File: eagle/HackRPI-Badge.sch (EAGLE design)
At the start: 42 parts, among them J1 FTDI_BASICPTH, J2 SOLDERJUMPERTRACE-PTH, U2 3.3V, U4 74595, U5 74595, U6 74595, U7 74165DT, U8 AT25SF041

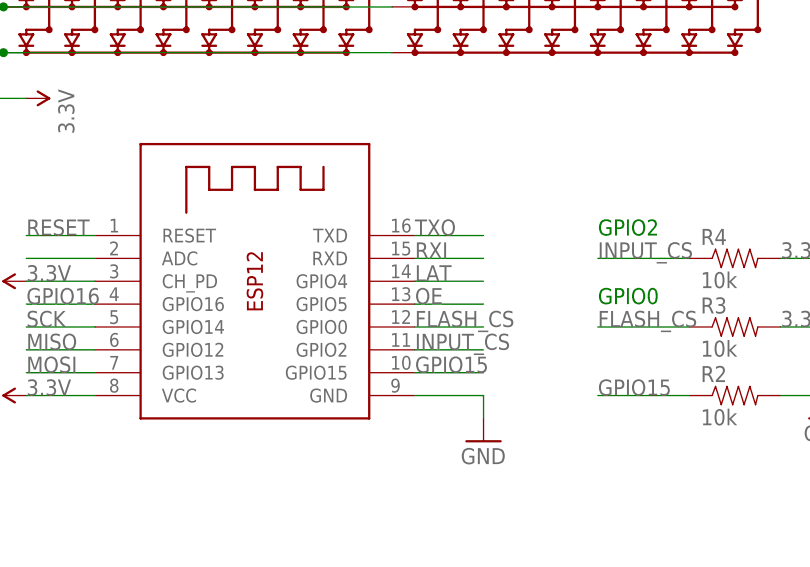
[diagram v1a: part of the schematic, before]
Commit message: Fixed ESP12 pinout
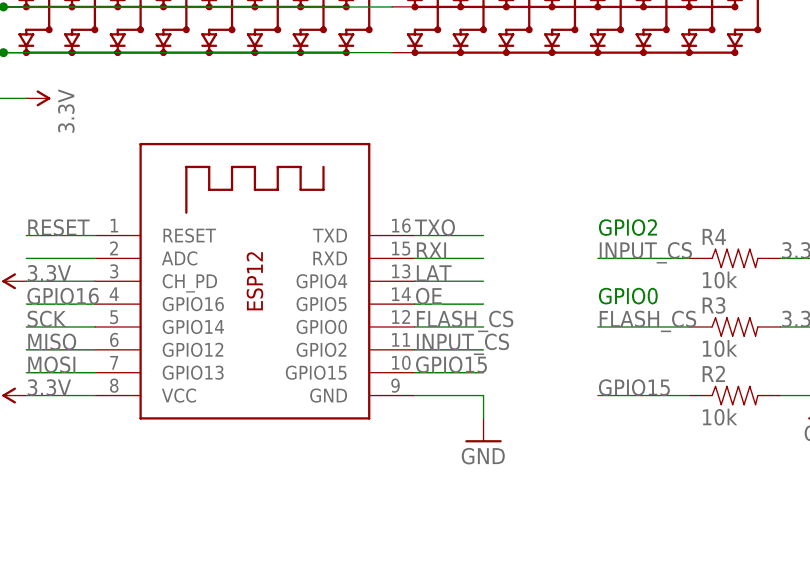
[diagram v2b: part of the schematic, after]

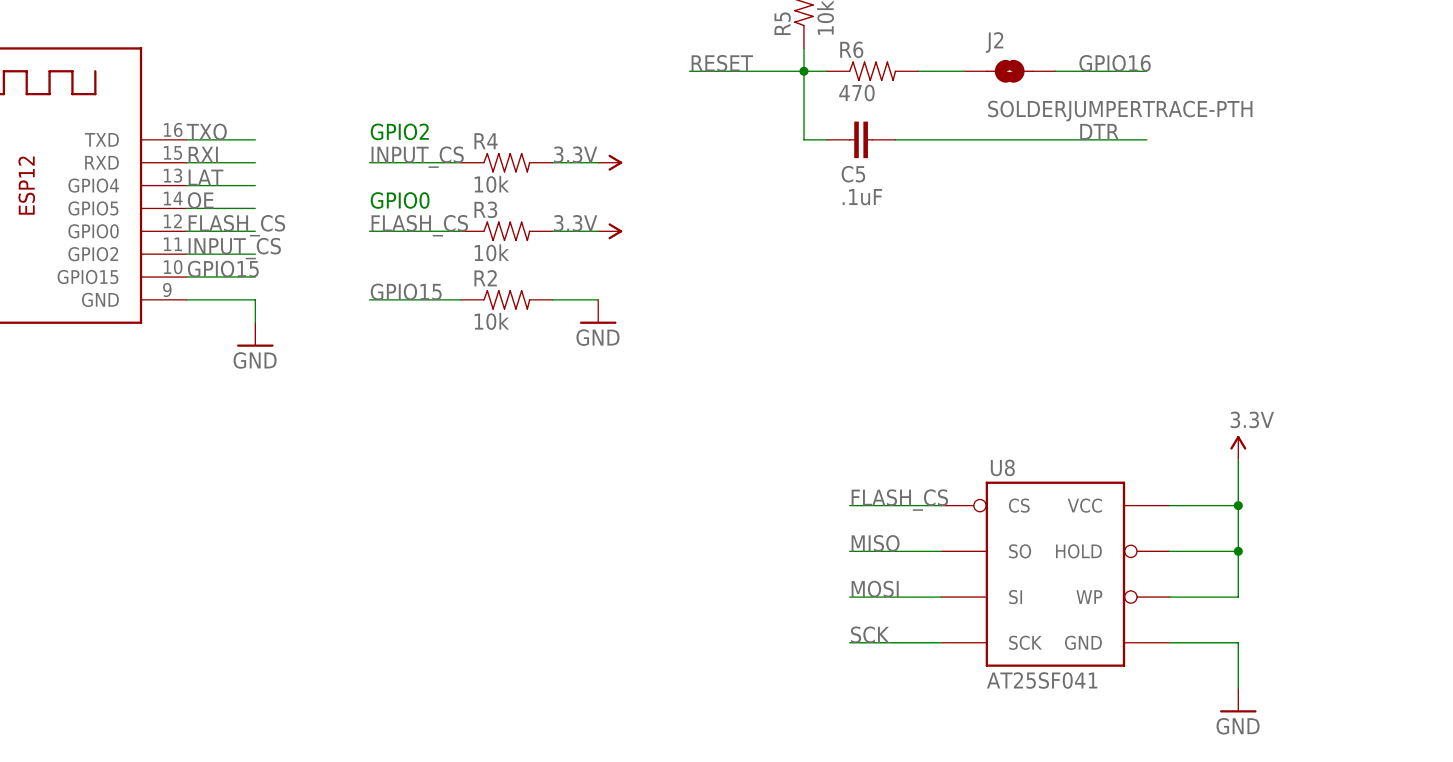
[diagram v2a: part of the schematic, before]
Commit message: Removed external flash memory from badge (ESP-12 module has plenty of flash onboard)
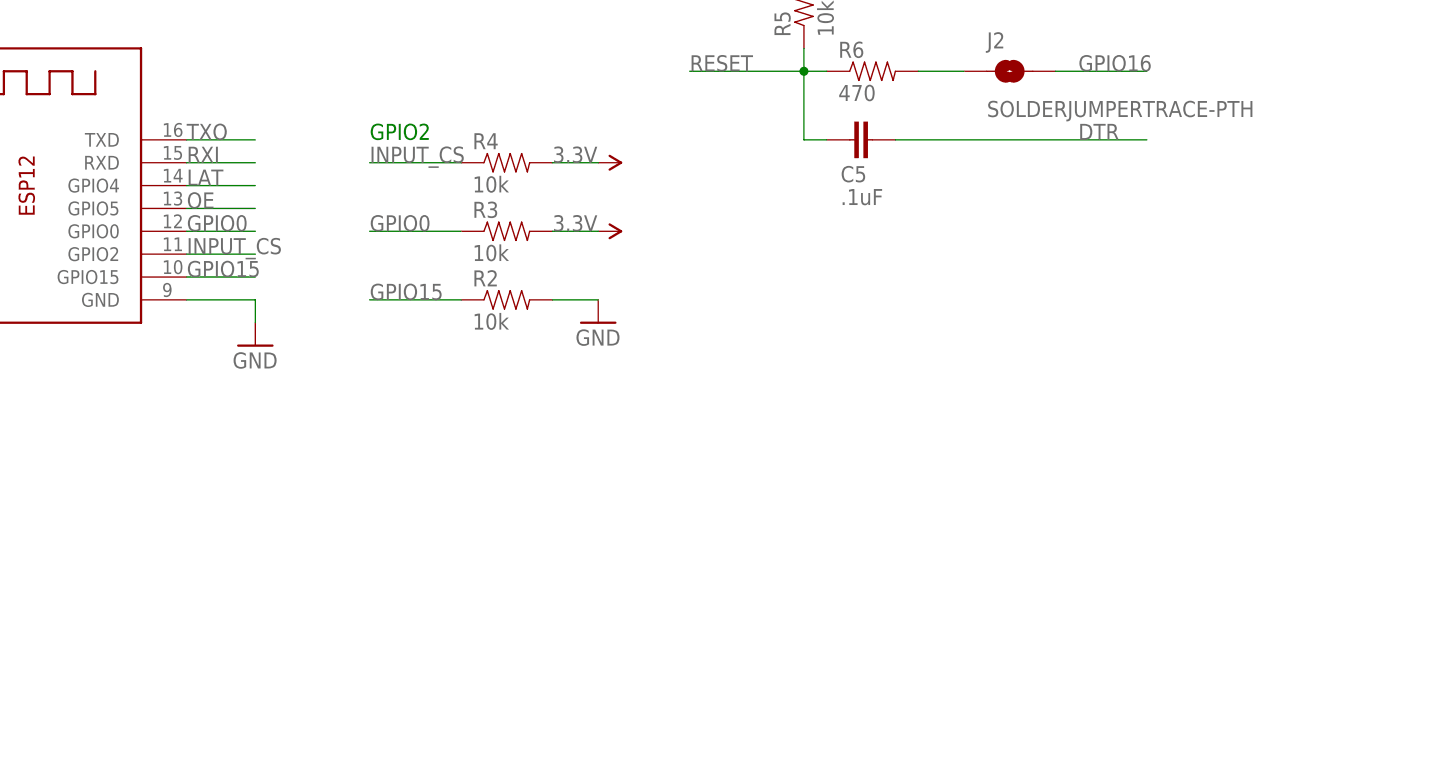
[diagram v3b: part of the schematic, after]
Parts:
- removed U8: AT25SF041, SparkFun-DigitalIC:AT25FS010
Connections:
- removed net FLASH_CS: R3.1, U1.GPIO0, U8.CS
- new net GPIO0: R3.1, U1.GPIO0
- net 3.3V: no longer U8.HOLD, U8.VCC, U8.WP
- net GND: no longer U8.GND
- net MISO: no longer U8.SO
- net MOSI: no longer U8.SI
- net SCK: no longer U8.SCK
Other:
- note removed: "GPIO0"
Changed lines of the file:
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@@
 <part name="GND17" library="SparkFun-Aesthetics" deviceset="GND" device=""/>
 <part name="SUPPLY23" library="SparkFun-Aesthetics" deviceset="V_BATT" device=""/>
-<part name="SUPPLY24" library="SparkFun-Aesthetics" deviceset="3.3V" device=""/>
-<part name="GND18" library="SparkFun-Aesthetics" deviceset="GND" device=""/>
-<part name="U8" library="SparkFun-DigitalIC" deviceset="AT25FS010" device="" value="AT25SF041">
-<attribute name="PARTNO" value="AT25SF041-SSHD-T"/>
-</part>
 </parts>
 <sheets>
 <sheet>
 <plain>
-<text x="38.1" y="-2.54" size="1.778" layer="91">GPIO0</text>
 <text x="38.1" y="5.08" size="1.778" layer="91">GPIO2</text>
 </plain>
@@
 <instance part="GND17" gate="1" x="-190.5" y="12.7"/>
 <instance part="SUPPLY23" gate="G$1" x="-190.5" y="45.72"/>
-<instance part="SUPPLY24" gate="G$1" x="134.62" y="-30.48"/>
-<instance part="GND18" gate="1" x="134.62" y="-58.42"/>
-<instance part="U8" gate="G$1" x="114.3" y="-40.64">
-<attribute name="PARTNO" x="114.3" y="-40.64" size="1.778" layer="96" display="off"/>
-</instance>
 </instances>
 <busses>
@@
 </segment>
 <segment>
-<wire x1="101.6" y1="-50.8" x2="91.44" y2="-50.8" width="0.1524" layer="91"/>
-<label x="91.44" y="-50.8" size="1.778" layer="95"/>
-<pinref part="U8" gate="G$1" pin="SCK"/>
-</segment>
-<segment>
 <pinref part="U7" gate="A" pin="CLK"/>
 <wire x1="104.14" y1="88.9" x2="91.44" y2="88.9" width="0.1524" layer="91"/>
@@
 <label x="91.44" y="81.28" size="1.778" layer="95"/>
 </segment>
-<segment>
-<wire x1="91.44" y1="-40.64" x2="101.6" y2="-40.64" width="0.1524" layer="91"/>
-<label x="91.44" y="-40.64" size="1.778" layer="95"/>
-<pinref part="U8" gate="G$1" pin="SO"/>
-</segment>
 </net>
 <net name="MOSI" class="0">
@@
 <wire x1="-111.76" y1="172.72" x2="-119.38" y2="172.72" width="0.1524" layer="91"/>
 <label x="-119.38" y="172.72" size="1.778" layer="95"/>
-</segment>
-<segment>
-<wire x1="101.6" y1="-45.72" x2="91.44" y2="-45.72" width="0.1524" layer="91"/>
-<label x="91.44" y="-45.72" size="1.778" layer="95"/>
-<pinref part="U8" gate="G$1" pin="SI"/>
 </segment>
 </net>
@@
 <wire x1="-88.9" y1="53.34" x2="-88.9" y2="50.8" width="0.1524" layer="91"/>
 </segment>
-<segment>
-<wire x1="127" y1="-35.56" x2="134.62" y2="-35.56" width="0.1524" layer="91"/>
-<wire x1="134.62" y1="-35.56" x2="134.62" y2="-30.48" width="0.1524" layer="91"/>
-<pinref part="SUPPLY24" gate="G$1" pin="3.3V"/>
-<wire x1="127" y1="-45.72" x2="134.62" y2="-45.72" width="0.1524" layer="91"/>
-<wire x1="134.62" y1="-45.72" x2="134.62" y2="-40.64" width="0.1524" layer="91"/>
-<junction x="134.62" y="-35.56"/>
-<pinref part="U8" gate="G$1" pin="WP"/>
-<pinref part="U8" gate="G$1" pin="VCC"/>
-<pinref part="U8" gate="G$1" pin="HOLD"/>
-<wire x1="134.62" y1="-40.64" x2="134.62" y2="-35.56" width="0.1524" layer="91"/>
-<wire x1="127" y1="-40.64" x2="134.62" y2="-40.64" width="0.1524" layer="91"/>
-<junction x="134.62" y="-40.64"/>
-</segment>
 </net>
 <net name="GND" class="1">
@@
 <pinref part="GND17" gate="1" pin="GND"/>
 </segment>
-<segment>
-<wire x1="127" y1="-50.8" x2="134.62" y2="-50.8" width="0.1524" layer="91"/>
-<wire x1="134.62" y1="-50.8" x2="134.62" y2="-55.88" width="0.1524" layer="91"/>
-<pinref part="GND18" gate="1" pin="GND"/>
-<pinref part="U8" gate="G$1" pin="GND"/>
-</segment>
 </net>
 <net name="INPUT_CS" class="0">
@@
 </segment>
 </net>
-<net name="FLASH_CS" class="0">
+<net name="GPIO0" class="0">
 <segment>
 <pinref part="U1" gate="G$1" pin="GPIO0"/>
@@
 <label x="38.1" y="-5.08" size="1.778" layer="95"/>
 </segment>
-<segment>
-<wire x1="101.6" y1="-35.56" x2="91.44" y2="-35.56" width="0.1524" layer="91"/>
-<label x="91.44" y="-35.56" size="1.778" layer="95"/>
-<pinref part="U8" gate="G$1" pin="CS"/>
-</segment>
-</net>
+</net>

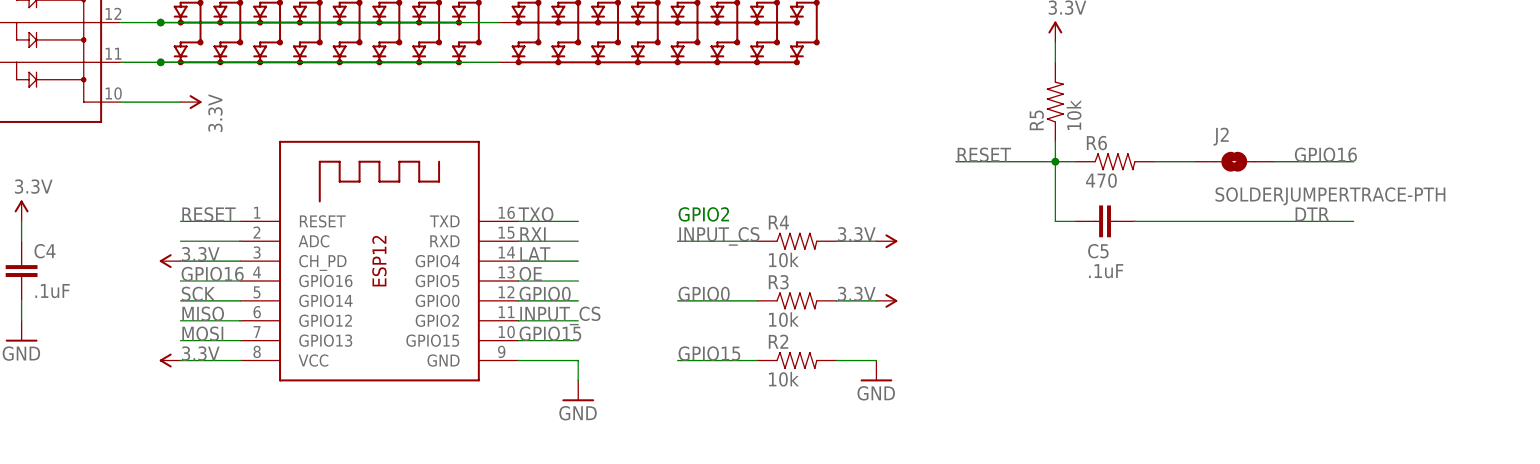
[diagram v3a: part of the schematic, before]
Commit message: Moved buttons, changed some pin assignments, added input shift register source
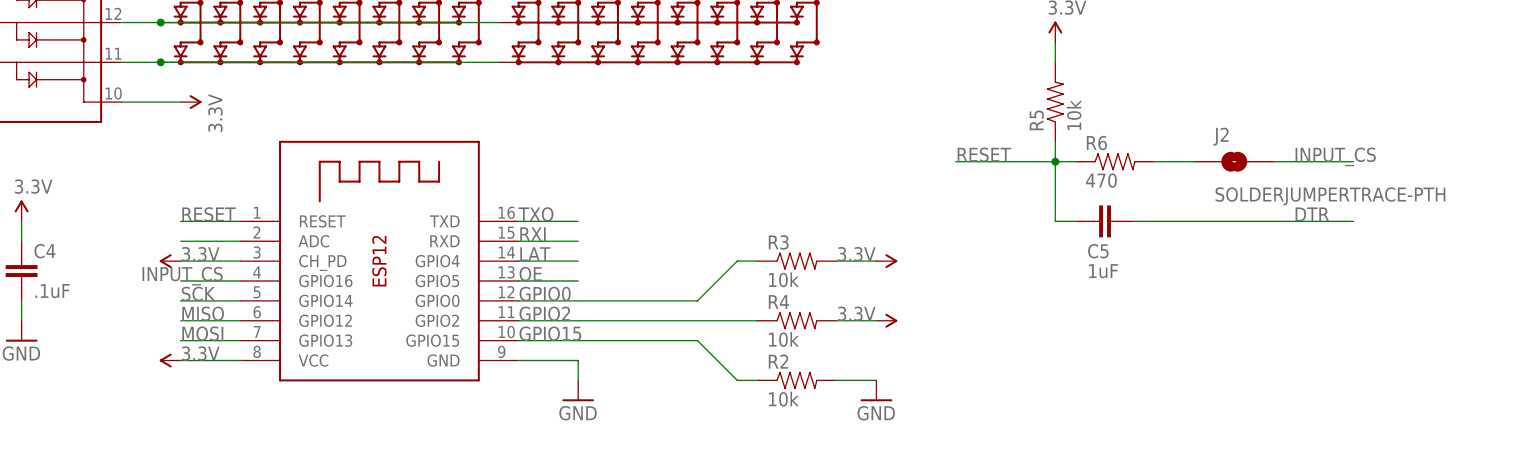
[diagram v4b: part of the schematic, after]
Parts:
- C5: value .1uF -> 1uF; PARTNO CC0603ZRY5V9BB104 -> (none)
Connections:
- removed net GPIO16: J2.2, U1.GPIO16
- new net GPIO2: R4.1, U1.GPIO2
- net INPUT_CS: now also J2.2, U1.GPIO16; no longer R4.1, U1.GPIO2
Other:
- note removed: "GPIO2"
- moved on the sheet: R2, R3, R4
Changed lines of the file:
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@@
 </part>
 <part name="J1" library="SparkFun-Connectors" deviceset="FTDI_BASIC" device="PTH"/>
-<part name="C5" library="SparkFun-Capacitors" deviceset="CAP" device="0603-CAP" value=".1uF">
-<attribute name="PARTNO" value="CC0603ZRY5V9BB104"/>
-</part>
+<part name="C5" library="SparkFun-Capacitors" deviceset="CAP" device="0603-CAP" value="1uF"/>
 <part name="J2" library="SparkFun-Retired" deviceset="SOLDERJUMPER" device="TRACE-PTH"/>
 <part name="U7" library="mylib" deviceset="74*165" device="DT">
@@
 <sheet>
 <plain>
-<text x="38.1" y="5.08" size="1.778" layer="91">GPIO2</text>
 </plain>
 <instances>
@@
 <attribute name="VALUE" x="-119.38" y="132.08" size="1.778" layer="96"/>
 </instance>
-<instance part="R2" gate="G$1" x="53.34" y="-12.7">
-<attribute name="PARTNO" x="53.34" y="-12.7" size="1.778" layer="96" display="off"/>
-</instance>
-<instance part="GND11" gate="1" x="63.5" y="-15.24"/>
+<instance part="R2" gate="G$1" x="53.34" y="-15.24">
+<attribute name="PARTNO" x="53.34" y="-15.24" size="1.778" layer="96" display="off"/>
+</instance>
+<instance part="GND11" gate="1" x="63.5" y="-17.78"/>
 <instance part="SUPPLY1" gate="G$1" x="-25.4" y="0" smashed="yes" rot="R90">
 <attribute name="VALUE" x="-25.4" y="0" size="1.778" layer="96"/>
 </instance>
-<instance part="SUPPLY16" gate="G$1" x="63.5" y="-5.08" smashed="yes" rot="R270">
-<attribute name="VALUE" x="58.42" y="-5.08" size="1.778" layer="96"/>
-</instance>
-<instance part="R3" gate="G$1" x="53.34" y="-5.08">
-<attribute name="PARTNO" x="53.34" y="-5.08" size="1.778" layer="96" display="off"/>
-</instance>
-<instance part="R4" gate="G$1" x="53.34" y="2.54">
-<attribute name="PARTNO" x="53.34" y="2.54" size="1.778" layer="96" display="off"/>
-</instance>
-<instance part="SUPPLY17" gate="G$1" x="63.5" y="2.54" smashed="yes" rot="R270">
-<attribute name="VALUE" x="58.42" y="2.54" size="1.778" layer="96"/>
+<instance part="SUPPLY16" gate="G$1" x="63.5" y="0" smashed="yes" rot="R270">
+<attribute name="VALUE" x="58.42" y="0" size="1.778" layer="96"/>
+</instance>
+<instance part="R3" gate="G$1" x="53.34" y="0">
+<attribute name="PARTNO" x="53.34" y="0" size="1.778" layer="96" display="off"/>
+</instance>
+<instance part="R4" gate="G$1" x="53.34" y="-7.62">
+<attribute name="PARTNO" x="53.34" y="-7.62" size="1.778" layer="96" display="off"/>
+</instance>
+<instance part="SUPPLY17" gate="G$1" x="63.5" y="-7.62" smashed="yes" rot="R270">
+<attribute name="VALUE" x="58.42" y="-7.62" size="1.778" layer="96"/>
 </instance>
 <instance part="R5" gate="G$1" x="86.36" y="20.32" rot="R90">
@@
 <attribute name="NAME" x="90.424" y="0.381" size="1.778" layer="95"/>
 <attribute name="VALUE" x="90.424" y="-2.159" size="1.778" layer="96"/>
-<attribute name="PARTNO" x="93.98" y="5.08" size="1.778" layer="96" display="off"/>
 </instance>
 <instance part="J2" gate="1" x="109.22" y="12.7"/>
@@
 </segment>
 <segment>
-<wire x1="58.42" y1="-5.08" x2="63.5" y2="-5.08" width="0.1524" layer="91"/>
+<wire x1="58.42" y1="0" x2="63.5" y2="0" width="0.1524" layer="91"/>
 <pinref part="SUPPLY16" gate="G$1" pin="3.3V"/>
 <pinref part="R3" gate="G$1" pin="2"/>
 </segment>
 <segment>
-<wire x1="58.42" y1="2.54" x2="63.5" y2="2.54" width="0.1524" layer="91"/>
+<wire x1="58.42" y1="-7.62" x2="63.5" y2="-7.62" width="0.1524" layer="91"/>
 <pinref part="SUPPLY17" gate="G$1" pin="3.3V"/>
 <pinref part="R4" gate="G$1" pin="2"/>
@@
 <pinref part="R2" gate="G$1" pin="2"/>
 <pinref part="GND11" gate="1" pin="GND"/>
-<wire x1="63.5" y1="-12.7" x2="58.42" y2="-12.7" width="0.1524" layer="91"/>
+<wire x1="63.5" y1="-15.24" x2="58.42" y2="-15.24" width="0.1524" layer="91"/>
 </segment>
 <segment>
@@
 <net name="INPUT_CS" class="0">
 <segment>
-<pinref part="U1" gate="G$1" pin="GPIO2"/>
-<wire x1="17.78" y1="-7.62" x2="25.4" y2="-7.62" width="0.1524" layer="91"/>
-<label x="17.78" y="-7.62" size="1.778" layer="95"/>
-</segment>
-<segment>
-<wire x1="38.1" y1="2.54" x2="48.26" y2="2.54" width="0.1524" layer="91"/>
-<pinref part="R4" gate="G$1" pin="1"/>
-<label x="38.1" y="2.54" size="1.778" layer="95"/>
-</segment>
-<segment>
 <pinref part="U7" gate="A" pin="CLK_INH"/>
 <wire x1="104.14" y1="86.36" x2="91.44" y2="86.36" width="0.1524" layer="91"/>
 <label x="91.44" y="86.36" size="1.778" layer="95"/>
 </segment>
+<segment>
+<pinref part="U1" gate="G$1" pin="GPIO16"/>
+<wire x1="-17.78" y1="-2.54" x2="-25.4" y2="-2.54" width="0.1524" layer="91"/>
+<label x="-30.48" y="-2.54" size="1.778" layer="95"/>
+</segment>
+<segment>
+<wire x1="124.46" y1="12.7" x2="114.3" y2="12.7" width="0.1524" layer="91"/>
+<label x="116.84" y="12.7" size="1.778" layer="95"/>
+<pinref part="J2" gate="1" pin="2"/>
+</segment>
 </net>
 <net name="GPIO0" class="0">
 <segment>
 <pinref part="U1" gate="G$1" pin="GPIO0"/>
-<wire x1="17.78" y1="-5.08" x2="25.4" y2="-5.08" width="0.1524" layer="91"/>
 <label x="17.78" y="-5.08" size="1.778" layer="95"/>
-</segment>
-<segment>
-<wire x1="38.1" y1="-5.08" x2="48.26" y2="-5.08" width="0.1524" layer="91"/>
+<wire x1="17.78" y1="-5.08" x2="40.64" y2="-5.08" width="0.1524" layer="91"/>
+<wire x1="40.64" y1="-5.08" x2="45.72" y2="0" width="0.1524" layer="91"/>
+<wire x1="45.72" y1="0" x2="48.26" y2="0" width="0.1524" layer="91"/>
 <pinref part="R3" gate="G$1" pin="1"/>
-<label x="38.1" y="-5.08" size="1.778" layer="95"/>
 </segment>
 </net>
@@
 <segment>
 <pinref part="U1" gate="G$1" pin="GPIO15"/>
-<wire x1="17.78" y1="-10.16" x2="25.4" y2="-10.16" width="0.1524" layer="91"/>
 <label x="17.78" y="-10.16" size="1.778" layer="95"/>
-</segment>
-<segment>
+<wire x1="17.78" y1="-10.16" x2="40.64" y2="-10.16" width="0.1524" layer="91"/>
+<wire x1="40.64" y1="-10.16" x2="45.72" y2="-15.24" width="0.1524" layer="91"/>
 <pinref part="R2" gate="G$1" pin="1"/>
-<wire x1="48.26" y1="-12.7" x2="38.1" y2="-12.7" width="0.1524" layer="91"/>
-<label x="38.1" y="-12.7" size="1.778" layer="95"/>
-</segment>
-</net>
-<net name="GPIO16" class="0">
-<segment>
-<pinref part="U1" gate="G$1" pin="GPIO16"/>
-<wire x1="-17.78" y1="-2.54" x2="-25.4" y2="-2.54" width="0.1524" layer="91"/>
-<label x="-25.4" y="-2.54" size="1.778" layer="95"/>
-</segment>
-<segment>
-<wire x1="124.46" y1="12.7" x2="114.3" y2="12.7" width="0.1524" layer="91"/>
-<label x="116.84" y="12.7" size="1.778" layer="95"/>
-<pinref part="J2" gate="1" pin="2"/>
+<wire x1="48.26" y1="-15.24" x2="45.72" y2="-15.24" width="0.1524" layer="91"/>
 </segment>
 </net>
@@
 </segment>
 </net>
+<net name="GPIO2" class="0">
+<segment>
+<pinref part="U1" gate="G$1" pin="GPIO2"/>
+<label x="17.78" y="-7.62" size="1.778" layer="95"/>
+<pinref part="R4" gate="G$1" pin="1"/>
+<wire x1="17.78" y1="-7.62" x2="48.26" y2="-7.62" width="0.1524" layer="91"/>
+</segment>
+</net>

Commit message: Tied GPIO0 to DTR, changed deep sleep jumper to normally open (necessary for programming)
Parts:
- J2: value SOLDERJUMPERTRACE-PTH -> SOLDERJUMPERPTH; device SparkFun-Retired:SOLDERJUMPERTRACE-PTH -> SparkFun-Retired:SOLDERJUMPERPTH
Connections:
- removed net GPIO0: R3.1, U1.GPIO0
- net DTR: now also R3.1, U1.GPIO0
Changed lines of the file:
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@@
 <part name="J1" library="SparkFun-Connectors" deviceset="FTDI_BASIC" device="PTH"/>
 <part name="C5" library="SparkFun-Capacitors" deviceset="CAP" device="0603-CAP" value="1uF"/>
-<part name="J2" library="SparkFun-Retired" deviceset="SOLDERJUMPER" device="TRACE-PTH"/>
+<part name="J2" library="SparkFun-Retired" deviceset="SOLDERJUMPER" device="PTH" value="SOLDERJUMPERPTH"/>
 <part name="U7" library="mylib" deviceset="74*165" device="DT">
 <attribute name="PARTNO" value="MC74HC165ADTR2G"/>
@@
 </segment>
 </net>
-<net name="GPIO0" class="0">
-<segment>
-<pinref part="U1" gate="G$1" pin="GPIO0"/>
-<label x="17.78" y="-5.08" size="1.778" layer="95"/>
-<wire x1="17.78" y1="-5.08" x2="40.64" y2="-5.08" width="0.1524" layer="91"/>
-<wire x1="40.64" y1="-5.08" x2="45.72" y2="0" width="0.1524" layer="91"/>
-<wire x1="45.72" y1="0" x2="48.26" y2="0" width="0.1524" layer="91"/>
-<pinref part="R3" gate="G$1" pin="1"/>
-</segment>
-</net>
 <net name="V_BATT" class="1">
 <segment>
@@
 <label x="-134.62" y="43.18" size="1.778" layer="95"/>
 </segment>
-</net>
+<segment>
+<pinref part="U1" gate="G$1" pin="GPIO0"/>
+<label x="17.78" y="-5.08" size="1.778" layer="95"/>
+<wire x1="17.78" y1="-5.08" x2="40.64" y2="-5.08" width="0.1524" layer="91"/>
+<wire x1="40.64" y1="-5.08" x2="45.72" y2="0" width="0.1524" layer="91"/>
+<wire x1="45.72" y1="0" x2="48.26" y2="0" width="0.1524" layer="91"/>
+<pinref part="R3" gate="G$1" pin="1"/>
+</segment>
+</net>
